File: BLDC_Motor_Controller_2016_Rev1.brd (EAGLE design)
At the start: 112.4 x 80 mm, 103 parts, among them J1 SERVOMOLEX_SL_THRU_HOLE, J3 APP_2POS_CONFIG5V_HORIZ, Q1 MOSFET-NCHANNELFQP30N06L, Q2 MOSFET-NCHANNELFQP30N06L, Q3 MOSFET-NCHANNELFQP30N06L, Q4 MOSFET-NCHANNELFQP30N06L, Q5 MOSFET-NCHANNELFQP30N06L, Q6 MOSFET-NCHANNELFQP30N06L, Q7 MOSFET-PCHANNEL, Q8 MOSFET-PCHANNEL

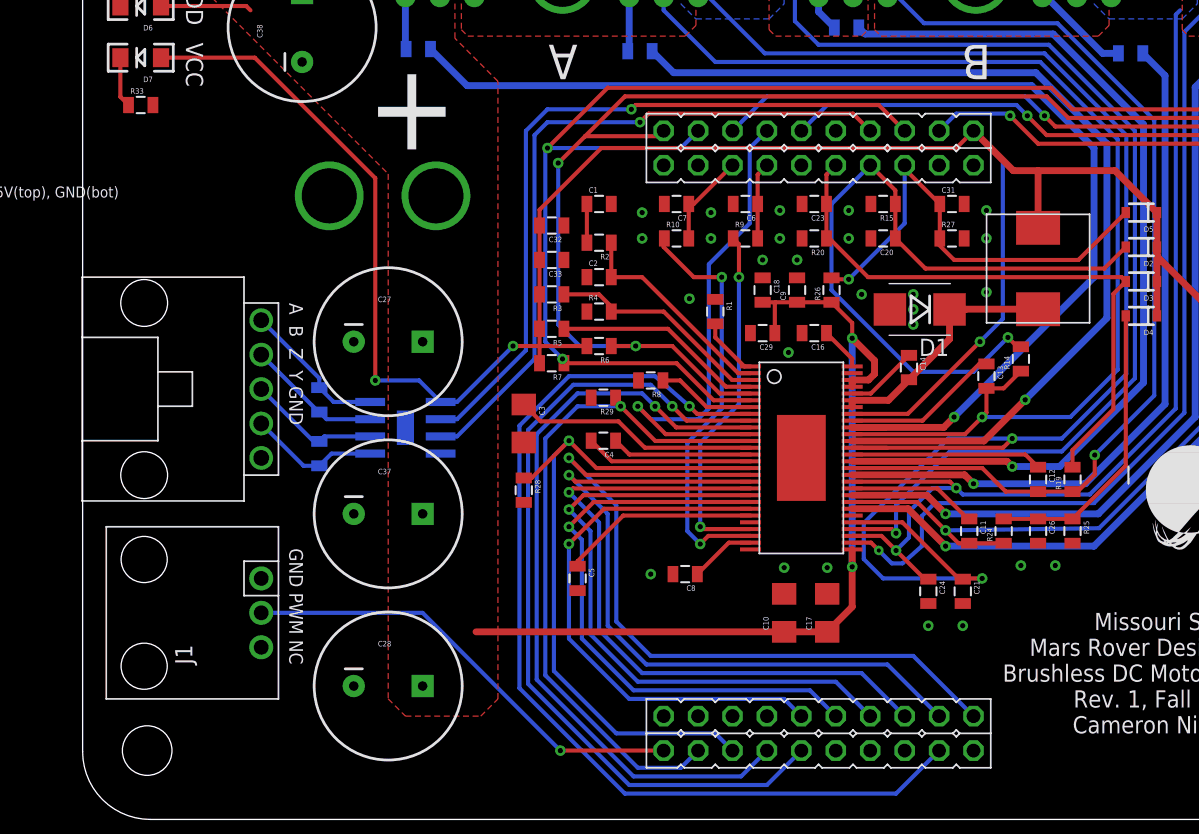
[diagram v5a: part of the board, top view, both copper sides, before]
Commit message: Half duplex RS485, single 5-pin SL connector on left side
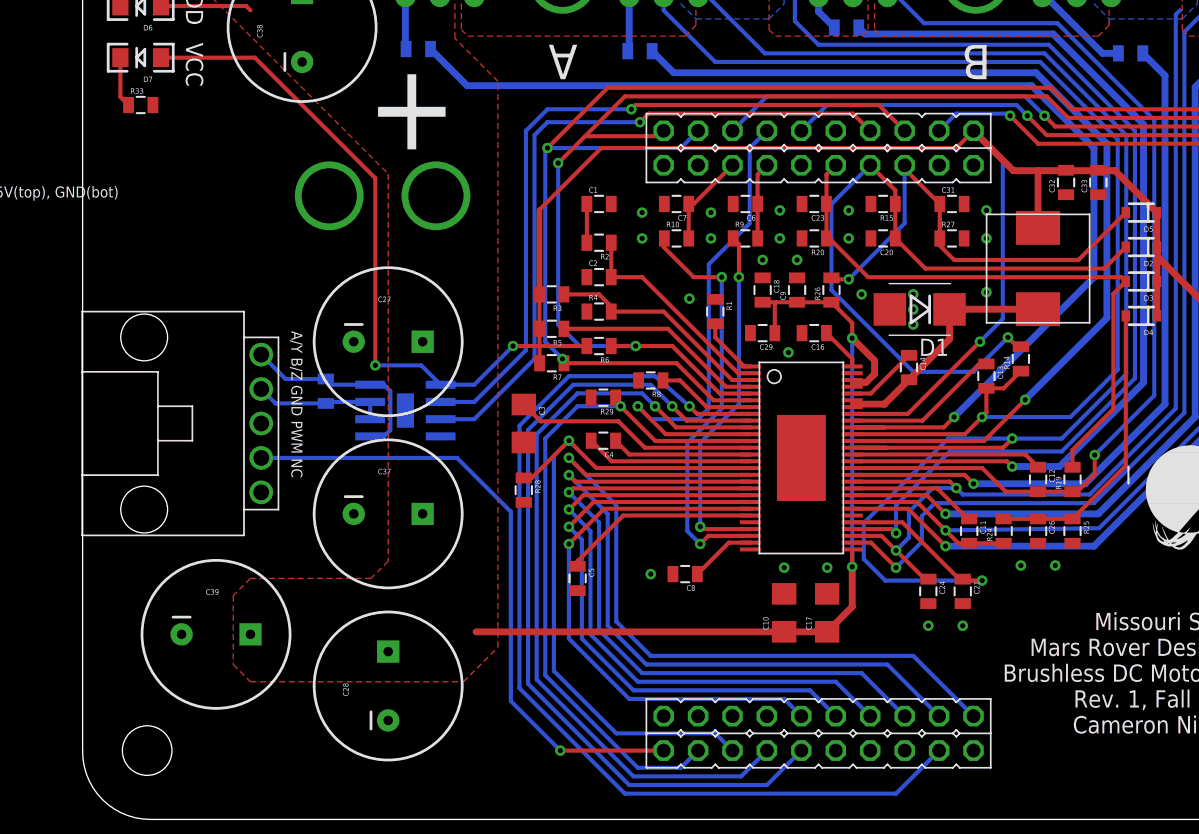
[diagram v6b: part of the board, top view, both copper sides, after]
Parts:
- removed J1: SERVOMOLEX_SL_THRU_HOLE, MRDT-Connectors:MOLEX_SL_03_THROUGH_HOLE
- removed R31: 3.3, SparkFun-Passives:0805
- added C39: 220u, SparkFun-Passives:CPOL-RADIAL-1000UF-25V
- R30: value 3.3 -> 120
- moved C33 40.7 mm to (72.7, 45.7), turned to 90 degrees
- moved C32 38.1 mm to (70.3, 45.7), turned to 90 degrees
- moved R30 4.63 mm to (15.7, 30.3)
- moved U$4 2.54 mm to (11.0, 27.9)
- moved U$3 1.27 mm to (21.6, 28.9)
- turned C28 to 90 degrees
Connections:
- removed net N$37: R31.2, U$3.7, U$4.2
- removed net N$38: R31.1, U$3.8, U$4.1
- net GND: now also C39.2, U$4.3; no longer J1.1, U$4.5
- net N$34: now also U$3.6, U$3.7, U$4.2; no longer U$3.5, U$4.4
- net N$36: now also U$3.5, U$3.8, U$4.1; no longer U$3.6, U$4.3
- net PVDD: now also C39.1
- net SPEED_IN: now also U$4.4; no longer J1.2
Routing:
- net SPEED_IN: track 33.9 -> 46.8 mm
- net N$38: track 10.9 -> 0.00 mm
- net N$37: track 10.0 -> 0.00 mm
- net N$36: track 9.79 -> 15.2 mm
- net VCC: track 232.6 -> 234.1 mm
- net TX: track 51.8 -> 51.2 mm
- net RX: track 54.1 -> 53.6 mm
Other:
- board text added: "A/Y B/Z GND PWM NC"
- board text removed: "A B Z Y GND"
- board text removed: "GND PWM NC"

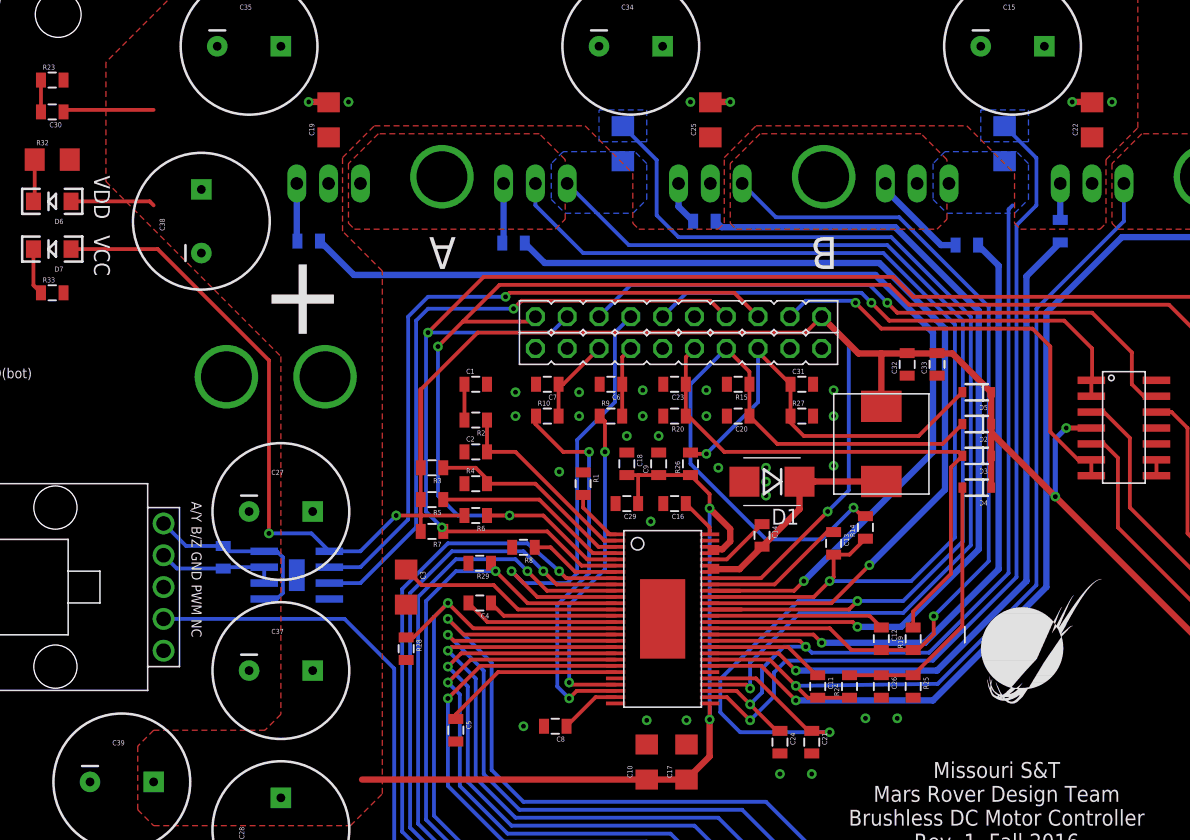
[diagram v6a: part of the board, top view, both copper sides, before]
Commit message: Routed separate sense resistor ground traces using short
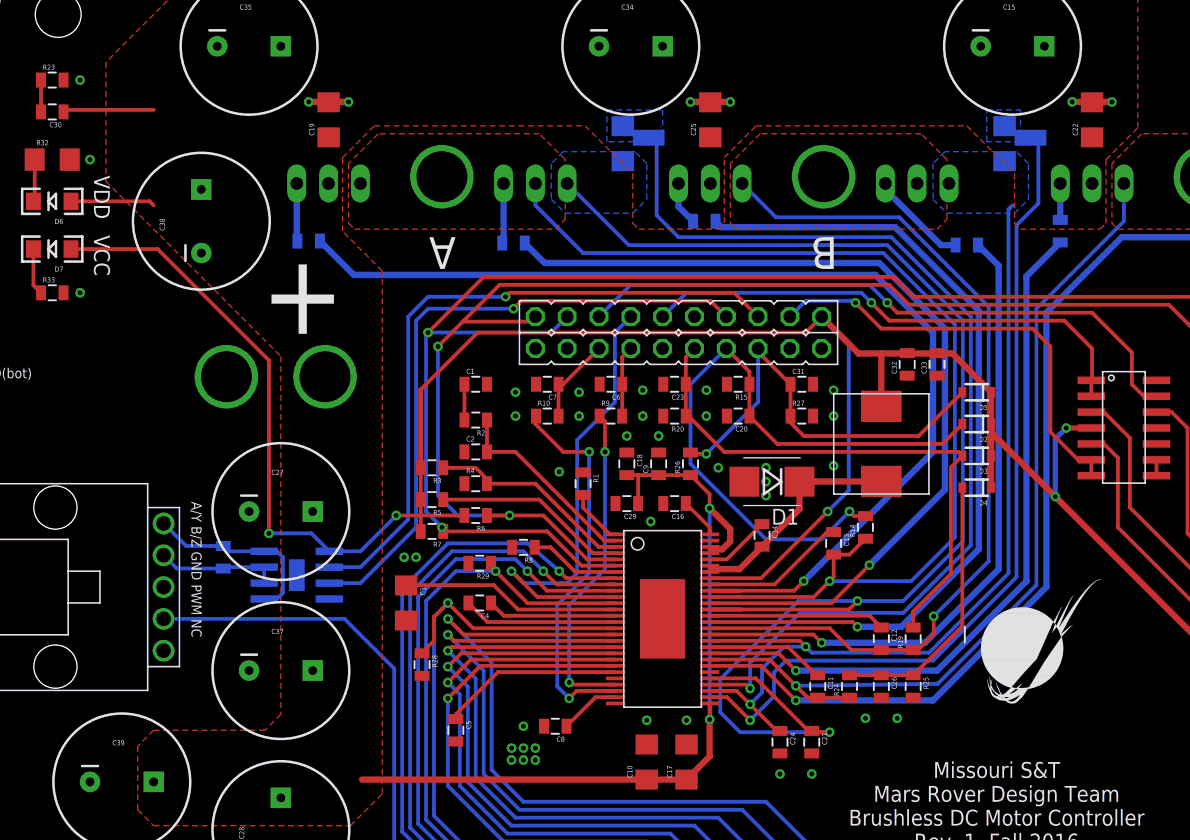
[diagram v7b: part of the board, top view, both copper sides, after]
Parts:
- added SH1, SH2: SHORT-HT5, shorts-old:SHORT_TOP-50
- moved R28 1.80 mm to (31.6, 21.7)
- moved C3 1.27 mm to (30.3, 26.7)
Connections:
- net GND: now also C21.2, C24.2, R13.1, R18.1, SH1.2, SH2.2
- net SP1: now also SH2.1; no longer C21.2, R13.1
- net SP2: now also SH1.1; no longer C24.2, R18.1
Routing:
- net GND: track 4.80 -> 14.4 mm, vias 34 -> 45
- net SP1: track 81.9 -> 79.8 mm
- net SP2: track 68.8 -> 66.9 mm
- net N$8: track 18.1 -> 17.5 mm

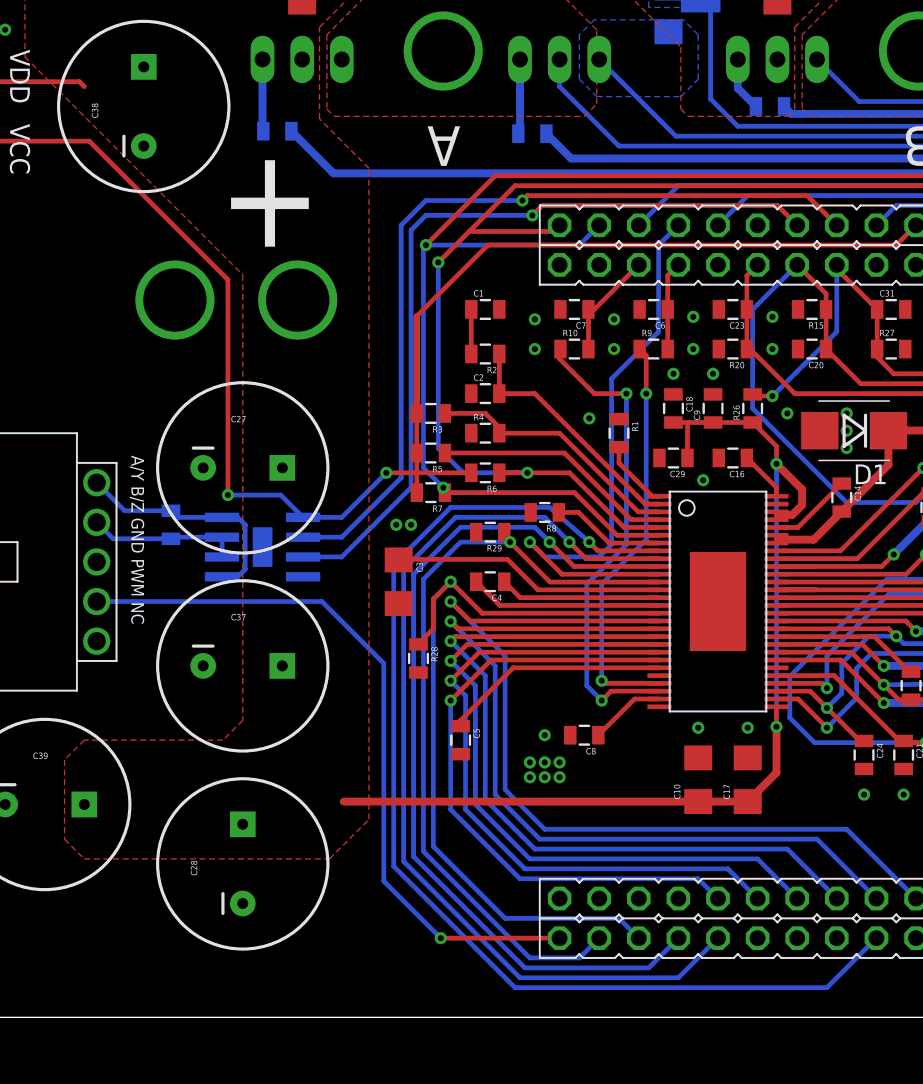
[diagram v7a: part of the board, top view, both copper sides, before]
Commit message: Swapped MAX3077 for MAX3078
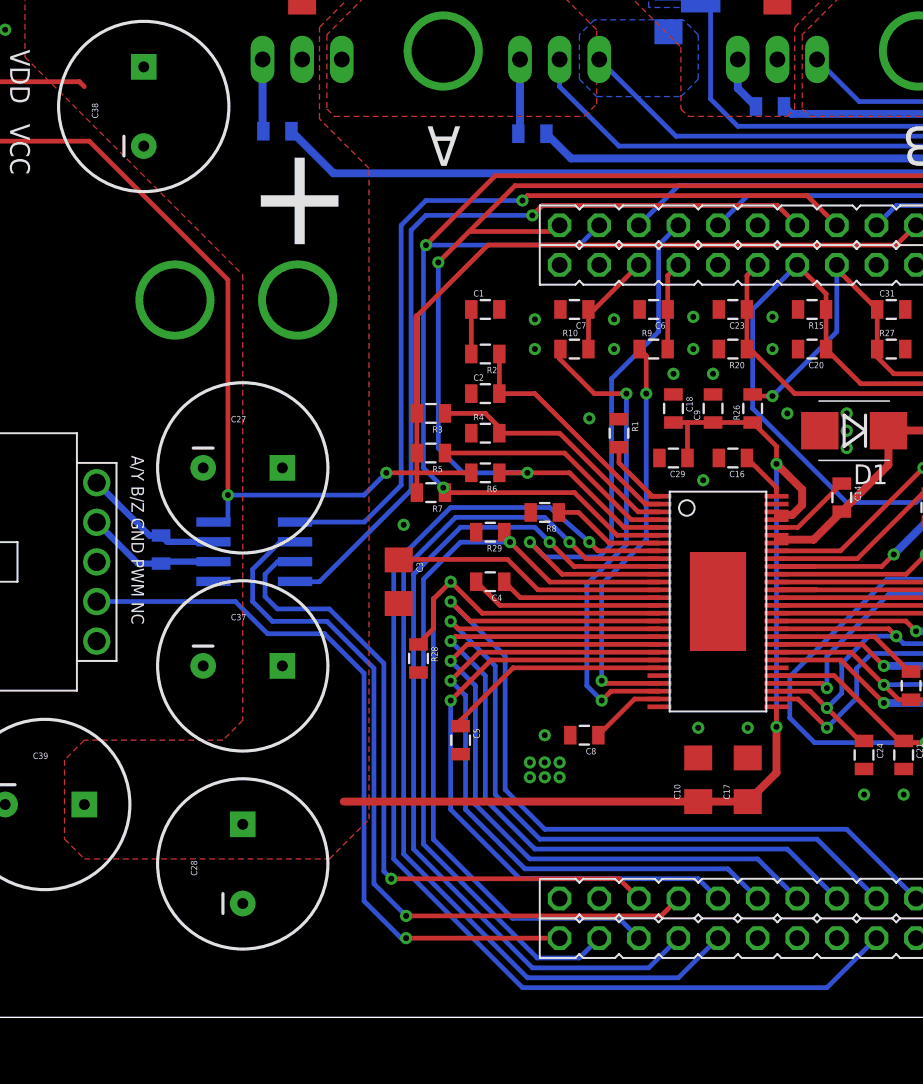
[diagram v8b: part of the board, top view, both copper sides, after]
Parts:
- removed U$3: MAX3077, MRDT-2015-General:SO8
- added U$10: MAX3078E, MRDT-ICs:SOIC8
- moved R30 1.71 mm to (15.1, 28.7)
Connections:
- new net DE: U$10.3, U$2.PD6
- new net NRE: U$10.2, U$2.PC7
- net GND: no longer U$3.4
- net N$34: now also U$10.6; no longer U$3.6, U$3.7
- net N$36: now also U$10.7; no longer U$3.5, U$3.8
- net RX: now also U$10.1; no longer U$3.2
- net TX: now also U$10.4; no longer U$3.3
- net VCC: now also U$10.8; no longer U$3.1
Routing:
- net NRE: track 0.00 -> 49.7 mm, vias 0 -> 1
- net DE: track 0.00 -> 43.5 mm, vias 0 -> 1
- net N$36: track 15.2 -> 9.06 mm
- net VCC: track 234.1 -> 235.6 mm
- net TX: track 51.2 -> 52.5 mm
- net N$34: track 9.79 -> 8.64 mm
- net GND: vias 45 -> 44
